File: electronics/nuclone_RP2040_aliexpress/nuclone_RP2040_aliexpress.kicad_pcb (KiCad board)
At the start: 2 copper layers, 50 x 76.2 mm, 22 parts, among them J1 JTAG_2X05, J3 nuclone_medium_left, J4 nuclone_medium_right, J5 Conn_02x06_Odd_Even, U1 RP2040_aliexpress

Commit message: prepared for production, updated versionnumber and components
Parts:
- N4: value NuClone Medium template V1.3 -> NuClone RP2040 aliexpress
- N5: value Nuclone Template V20240211 -> Nuclone Template V20240218
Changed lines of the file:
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@@
     (property "ki_keywords" "R res resistor")
     (attr smd)
-    (fp_text reference "R3" (at 1.9 -1.1) (layer "F.SilkS")
+    (fp_text reference "R3" (at 1.9 -0.4) (layer "F.SilkS")
         (effects (font (size 0.8 0.8) (thickness 0.15)))
     )
@@
     (property "ki_keywords" "R res resistor")
     (attr smd)
-    (fp_text reference "R5" (at 1.9 -0.3) (layer "F.SilkS")
+    (fp_text reference "R5" (at 1.9 0.4) (layer "F.SilkS")
         (effects (font (size 0.8 0.8) (thickness 0.15)))
     )
@@
     (property "ki_keywords" "R res resistor")
     (attr smd)
-    (fp_text reference "R6" (at 1.9 0.1) (layer "F.SilkS")
+    (fp_text reference "R6" (at 1.9 0.8) (layer "F.SilkS")
         (effects (font (size 0.8 0.8) (thickness 0.15)))
     )
@@
         (effects (font (size 1 1) (thickness 0.15)))
     )
-    (fp_text value "NuClone Medium template V1.3" (at 0 0.0125) (layer "F.SilkS")
+    (fp_text value "NuClone RP2040 aliexpress" (at 0 0.0125) (layer "F.SilkS")
         (effects (font (size 0.8 0.8) (thickness 0.15)))
     )
@@
     (property "ki_keywords" "medium nuclone right")
     (attr through_hole)
-    (fp_text reference "J4" (at -22.86 -6.985) (layer "F.SilkS")
+    (fp_text reference "J4" (at -26.14 -0.01) (layer "F.SilkS")
         (effects (font (size 0.8 0.8) (thickness 0.15)))
     )
@@
     (property "ki_keywords" "R res resistor")
     (attr smd)
-    (fp_text reference "R2" (at 1.9 -1.5) (layer "F.SilkS")
+    (fp_text reference "R2" (at 1.9 -0.8) (layer "F.SilkS")
         (effects (font (size 0.8 0.8) (thickness 0.15)))
     )
@@
     (property "ki_keywords" "R res resistor")
     (attr smd)
-    (fp_text reference "R4" (at 1.9 -0.7) (layer "F.SilkS")
+    (fp_text reference "R4" (at 1.9 0) (layer "F.SilkS")
         (effects (font (size 0.8 0.8) (thickness 0.15)))
     )
@@
     (property "Sheetname" "microcontroller")
     (attr through_hole)
-    (fp_text reference "U1" (at 11.2 -22.2 unlocked) (layer "F.SilkS")
-        (effects (font (size 1 1) (thickness 0.15)))
+    (fp_text reference "U1" (at 9.6 31.2 unlocked) (layer "F.SilkS")
+        (effects (font (size 0.8 0.8) (thickness 0.15)))
     )
     (fp_text value "RP2040_aliexpress" (at 0 15.24 unlocked) (layer "F.Fab")
-        (effects (font (size 1 1) (thickness 0.15)))
+        (effects (font (size 0.8 0.8) (thickness 0.15)))
+    )
+    (fp_text user "VIN" (at 11.43 -16.51 unlocked) (layer "F.SilkS")
+        (effects (font (size 0.8 0.8) (thickness 0.15)))
+    )
+    (fp_text user "GP14" (at -11.811 21.59 unlocked) (layer "F.SilkS")
+        (effects (font (size 0.8 0.8) (thickness 0.15)))
+    )
+    (fp_text user "GP10" (at -11.811 8.89 unlocked) (layer "F.SilkS")
+        (effects (font (size 0.8 0.8) (thickness 0.15)))
+    )
+    (fp_text user "GP4" (at -11.43 -8.89 unlocked) (layer "F.SilkS")
+        (effects (font (size 0.8 0.8) (thickness 0.15)))
+    )
+    (fp_text user "GP13" (at -11.811 19.05 unlocked) (layer "F.SilkS")
+        (effects (font (size 0.8 0.8) (thickness 0.15)))
+    )
+    (fp_text user "GP3" (at -11.43 -11.43 unlocked) (layer "F.SilkS")
+        (effects (font (size 0.8 0.8) (thickness 0.15)))
+    )
+    (fp_text user "GP15" (at -11.811 24.13 unlocked) (layer "F.SilkS")
+        (effects (font (size 0.8 0.8) (thickness 0.15)))
+    )
+    (fp_text user "GP6" (at -11.43 -1.27 unlocked) (layer "F.SilkS")
+        (effects (font (size 0.8 0.8) (thickness 0.15)))
+    )
+    (fp_text user "SWCLK" (at 1.27 32.512 90 unlocked) (layer "F.SilkS")
+        (effects (font (size 0.8 0.8) (thickness 0.15)))
+    )
+    (fp_text user "GP11" (at -11.811 11.43 unlocked) (layer "F.SilkS")
+        (effects (font (size 0.8 0.8) (thickness 0.15)))
+    )
+    (fp_text user "GP9" (at -11.43 6.35 unlocked) (layer "F.SilkS")
+        (effects (font (size 0.8 0.8) (thickness 0.15)))
+    )
+    (fp_text user "GND" (at -11.43 16.51 unlocked) (layer "F.SilkS")
+        (effects (font (size 0.8 0.8) (thickness 0.15)))
+    )
+    (fp_text user "GP8" (at -11.43 3.81 unlocked) (layer "F.SilkS")
+        (effects (font (size 0.8 0.8) (thickness 0.15)))
+    )
+    (fp_text user "GP5" (at -11.43 -3.81 unlocked) (layer "F.SilkS")
+        (effects (font (size 0.8 0.8) (thickness 0.15)))
     )
     (fp_text user "SWIO" (at 3.81 32.004 90 unlocked) (layer "F.SilkS")
         (effects (font (size 0.8 0.8) (thickness 0.15)))
     )
+    (fp_text user "GP17" (at -11.811 29.21 unlocked) (layer "F.SilkS")
+        (effects (font (size 0.8 0.8) (thickness 0.15)))
+    )
+    (fp_text user "GND" (at -1.27 31.75 90 unlocked) (layer "F.SilkS")
+        (effects (font (size 0.8 0.8) (thickness 0.15)))
+    )
+    (fp_text user "VBUS" (at 11.811 -19.05 unlocked) (layer "F.SilkS")
+        (effects (font (size 0.8 0.8) (thickness 0.15)))
+    )
+    (fp_text user "GP12" (at -11.811 13.97 unlocked) (layer "F.SilkS")
+        (effects (font (size 0.8 0.8) (thickness 0.15)))
+    )
     (fp_text user "3V3" (at -3.81 31.75 90 unlocked) (layer "F.SilkS")
         (effects (font (size 0.8 0.8) (thickness 0.15)))
     )
-    (fp_text user "SWCLK" (at 1.27 32.512 90 unlocked) (layer "F.SilkS")
-        (effects (font (size 0.8 0.8) (thickness 0.15)))
-    )
-    (fp_text user "GND" (at -1.27 31.75 90 unlocked) (layer "F.SilkS")
+    (fp_text user "GND" (at -11.43 -6.35 unlocked) (layer "F.SilkS")
+        (effects (font (size 0.8 0.8) (thickness 0.15)))
+    )
+    (fp_text user "GP7" (at -11.43 1.27 unlocked) (layer "F.SilkS")
+        (effects (font (size 0.8 0.8) (thickness 0.15)))
+    )
+    (fp_text user "GP16" (at -11.811 26.67 unlocked) (layer "F.SilkS")
         (effects (font (size 0.8 0.8) (thickness 0.15)))
     )
     (fp_text user "USB-C" (at 0 -21.59 unlocked) (layer "Eco1.User")
-        (effects (font (size 1 1) (thickness 0.15)))
+        (effects (font (size 0.8 0.8) (thickness 0.15)))
     )
     (fp_text user "${REFERENCE}" (at 0 12.7 unlocked) (layer "F.Fab")
-        (effects (font (size 1 1) (thickness 0.15)))
+        (effects (font (size 0.8 0.8) (thickness 0.15)))
     )
     (fp_line (start -10.16 -20.32) (end -10.16 -19.05)
@@
         (effects (font (size 1 1) (thickness 0.15)) (justify mirror))
     )
-    (fp_text value "Nuclone Template V20240211" (at 0.8 0.23) (layer "B.SilkS")
+    (fp_text value "Nuclone Template V20240218" (at 0.8 0.23) (layer "B.SilkS")
         (effects (font (size 0.8 0.8) (thickness 0.15)) (justify mirror))
     )

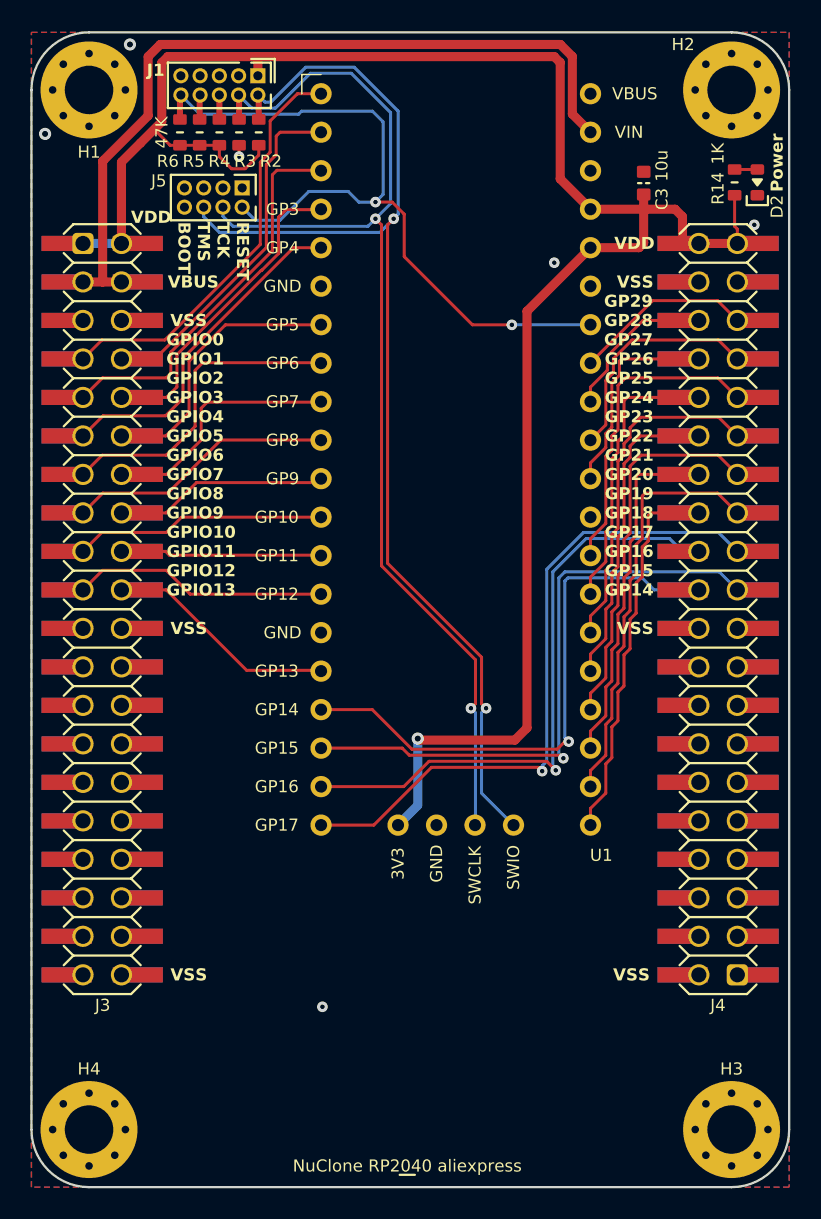
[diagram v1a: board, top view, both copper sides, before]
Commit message: moved RP2040 module so it does not collide with SWD/JTAG connector
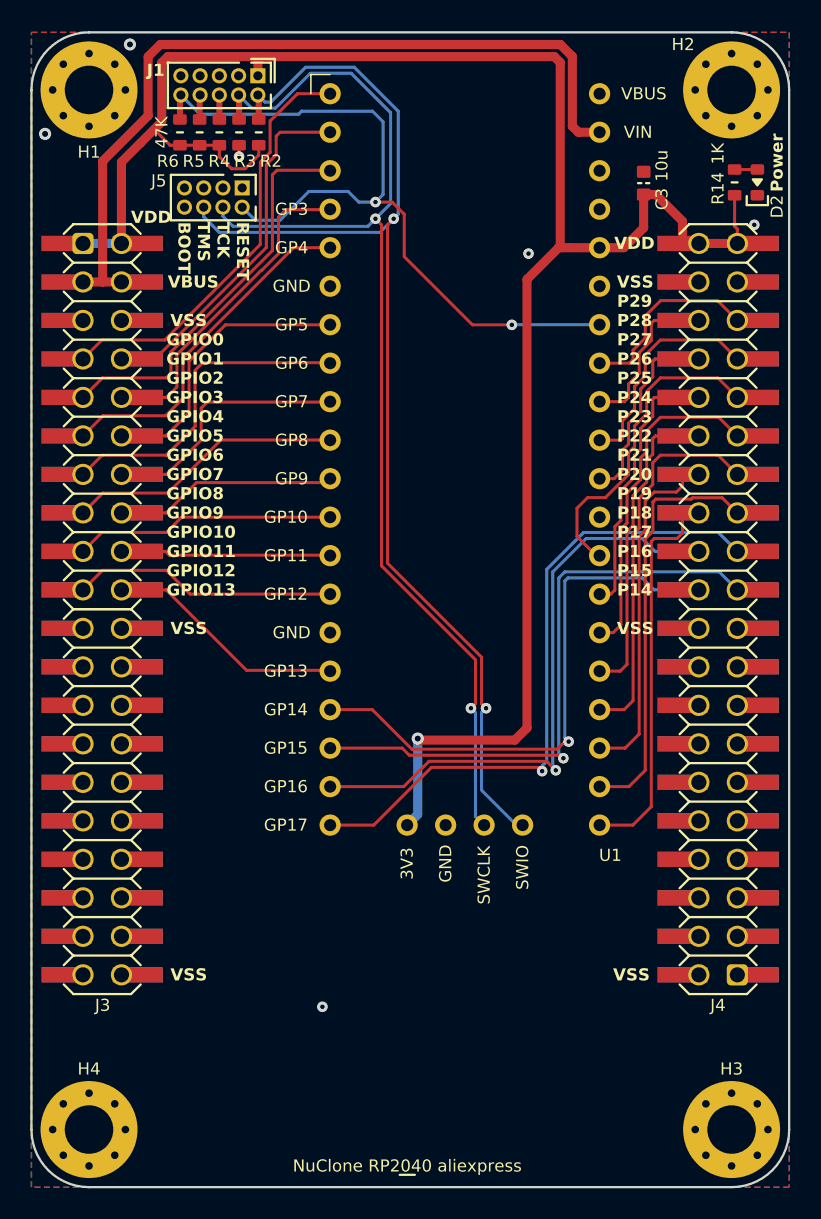
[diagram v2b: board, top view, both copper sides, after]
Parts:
- moved U1 0.60 mm to (88.7, 84.1)
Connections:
- U1 pad 37: /VDD -> unconnected-(U1-3V3_EN-Pad37)
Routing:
- net /VDD: track 132.6 -> 131.5 mm
- net /VBUS: track 52.8 -> 53.9 mm
- net /GPIO_58: track 12.8 -> 11.8 mm
- net /GPIO_56: track 17.6 -> 16.8 mm
- net /GPIO_50: track 24.3 -> 25.0 mm
- net /GPIO_61: track 12.0 -> 12.6 mm
- net /GPIO_47: track 40.7 -> 40.1 mm
- net /RESET: track 50.8 -> 51.4 mm
- net /GPIO_49: track 43.8 -> 43.2 mm
- net /GPIO_48: track 39.4 -> 38.8 mm
- net /GPIO_46: track 36.5 -> 35.9 mm
- net /GPIO_13: track 14.3 -> 14.9 mm
- net /GPIO_12: track 16.9 -> 17.5 mm
- net /GPIO_10: track 16.6 -> 17.2 mm
- net /GPIO_04: track 22.4 -> 23.0 mm
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
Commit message: reviewed and small fixes
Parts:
- N2: value V20240114 -> V20240424
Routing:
- net /GPIO_01: track 22.8 -> 21.8 mm
- net /VDD: track 131.5 -> 132.3 mm
- net /GPIO_00: track 28.0 -> 27.2 mm
- net /VSS: vias 6 -> 11

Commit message: preparing for production final checks
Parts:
- N2: value V20240424 -> V20240426
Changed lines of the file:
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@@
         (effects (font (size 1 1) (thickness 0.15)) (justify mirror))
     )
-    (fp_text value "V20240424" (at -0.05 0.1) (layer "B.SilkS")
+    (fp_text value "V20240426" (at -0.05 0.1) (layer "B.SilkS")
         (effects (font (size 0.8 0.8) (thickness 0.15)) (justify mirror))
     )
